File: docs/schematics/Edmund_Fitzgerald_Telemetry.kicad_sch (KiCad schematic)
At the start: 13 parts, among them Q1 MOSFET_N, Q2 MOSFET_N, U1 ESP32_Control, U2 MAX98357A, U3 DFPlayer_Pro

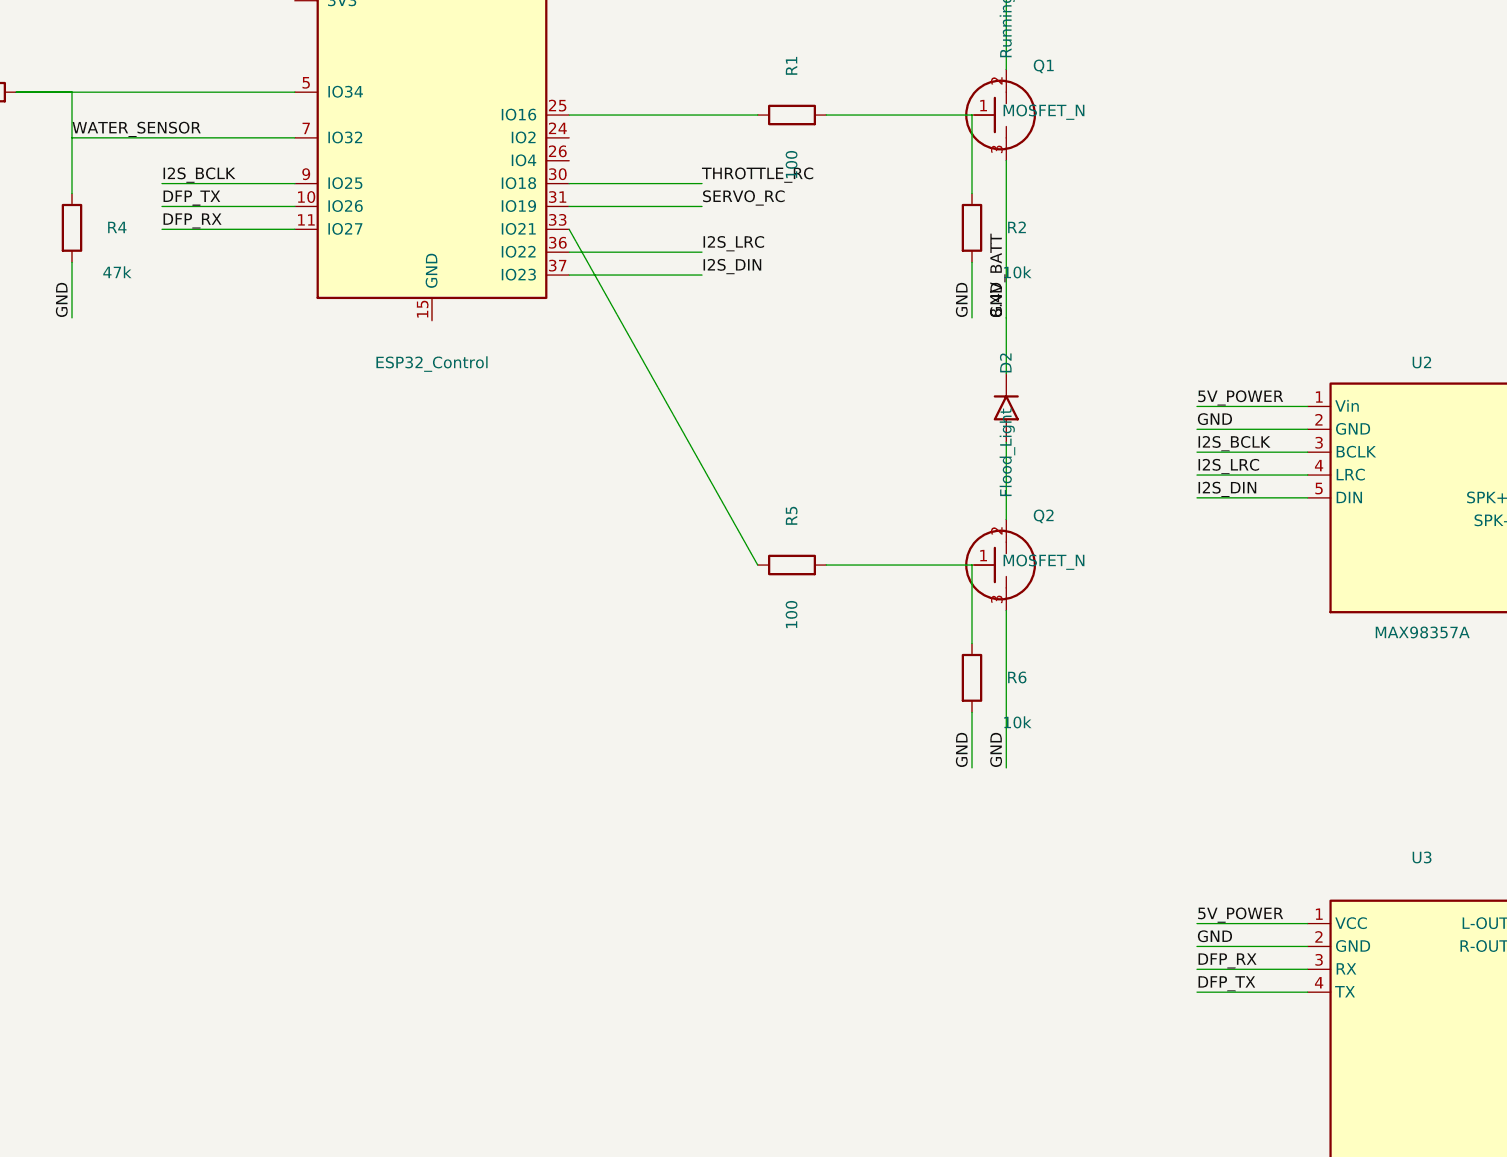
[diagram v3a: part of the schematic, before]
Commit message: Complete consolidated KiCAD schematic v3.0
- All components (ESP32, MOSFETs, Sensors, Audio) restored
- Physical orthogonal wiring between ESP32 and Audio modules
- Fixed all component labeling (no more ? symbols)
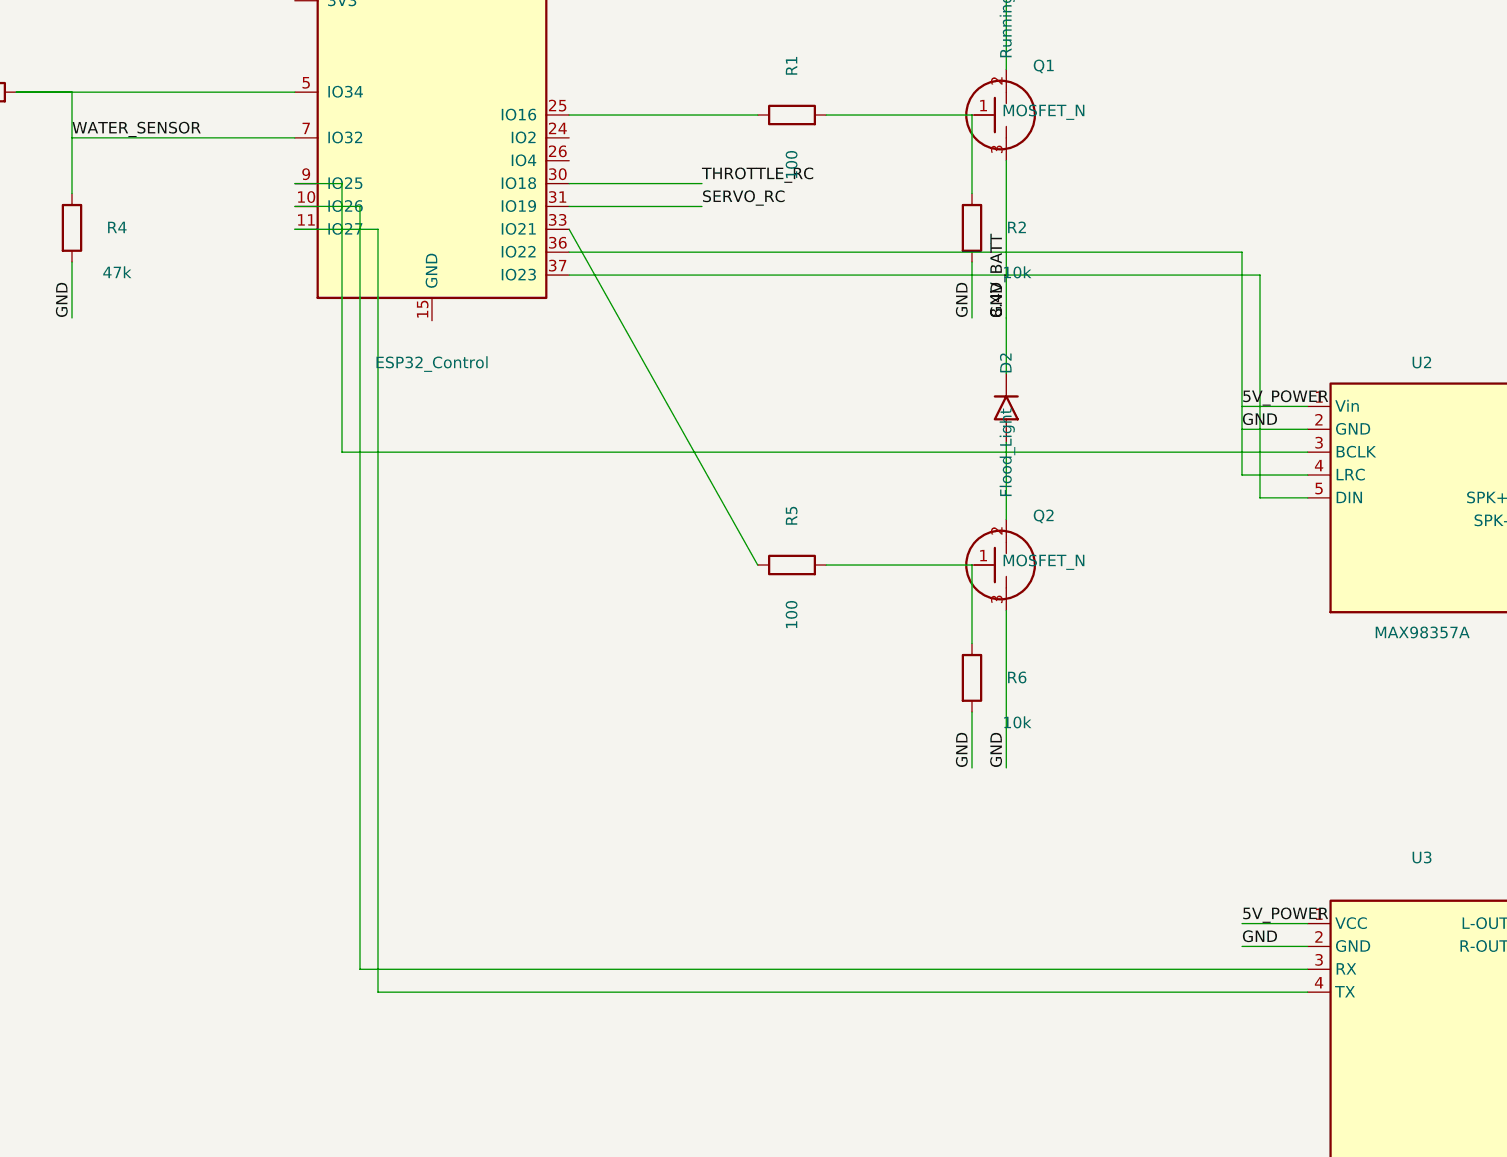
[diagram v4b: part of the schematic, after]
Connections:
- net 8.4V_BATT is gone; now on net 5V_POWER: D1.2 (A), D2.2 (A), Q1.3 (S), Q2.3 (S), R2.2, R3.1, R4.2, R6.2, U2.2 (GND), U3.2 (GND)
- net I2S_LRC is gone; now on net 5V_POWER: U1.36 (IO22), U2.4 (LRC)
- net DFP_RX: no longer names the net of U3.3 (RX)
- net DFP_RX: now also U1.10 (IO26); no longer U1.11 (IO27)
- net DFP_TX: no longer names the net of U3.4 (TX)
- net DFP_TX: now also U1.11 (IO27); no longer U1.10 (IO26)
- net I2S_BCLK: no longer names the net of U1.9 (IO25), U2.3 (BCLK)
- net I2S_DIN: no longer names the net of U1.37 (IO23), U2.5 (DIN)
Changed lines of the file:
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@@
 (kicad_sch (version 20230121) (generator eeschema)
  (paper "A3")
- (title_block (title "Edmund Fitzgerald - FULL SYSTEM") (company "Project Edmund Fitzgerald") (rev "2.0") (date "2026-01-31"))
+ (title_block (title "Edmund Fitzgerald - FULL SYSTEM") (company "Project Edmund Fitzgerald") (rev "2.3") (date "2026-01-31"))
  (symbol (lib_id "MCU_Espressif:ESP32-WROOM-32") (at 150 100 0) (unit 1) (in_bom yes) (on_board yes) (fields_autoplaced yes) (property "Reference" "U1" (at 150 75 0)) (property "Value" "ESP32_Control" (at 150 125 0)))
  (symbol (lib_id "Transistor_FET:Q_NMOS_GDS") (at 210 97.46 0) (unit 1) (in_bom yes) (on_board yes) (property "Reference" "Q1" (at 218 92 0)) (property "Value" "MOSFET_N" (at 218 97 0)))
@@
  (symbol (lib_id "Module:MAX98357A") (at 260 140 0) (unit 1) (in_bom yes) (on_board yes) (property "Reference" "U2" (at 260 125 0)) (property "Value" "MAX98357A" (at 260 155 0)))
  (symbol (lib_id "Module:DFPlayer_Pro") (at 260 200 0) (unit 1) (in_bom yes) (on_board yes) (property "Reference" "U3" (at 260 180 0)) (property "Value" "DFPlayer_Pro" (at 260 220 0)))
-  (wire (pts (xy 247.3 129.84) (xy 235 129.84)) (stroke (width 0) (type solid)))
-  (label "5V_POWER" (at 235 129.84 0) (effects (font (size 1.27 1.27)) (justify left bottom)))
-  (wire (pts (xy 247.3 132.38) (xy 235 132.38)) (stroke (width 0) (type solid)))
-  (label "GND" (at 235 132.38 0) (effects (font (size 1.27 1.27)) (justify left bottom)))
-  (wire (pts (xy 247.3 134.92) (xy 235 134.92)) (stroke (width 0) (type solid)))
-  (label "I2S_BCLK" (at 235 134.92 0) (effects (font (size 1.27 1.27)) (justify left bottom)))
-  (wire (pts (xy 247.3 137.46) (xy 235 137.46)) (stroke (width 0) (type solid)))
-  (label "I2S_LRC" (at 235 137.46 0) (effects (font (size 1.27 1.27)) (justify left bottom)))
-  (wire (pts (xy 247.3 140.0) (xy 235 140.0)) (stroke (width 0) (type solid)))
-  (label "I2S_DIN" (at 235 140.0 0) (effects (font (size 1.27 1.27)) (justify left bottom)))
-  (wire (pts (xy 247.3 187.3) (xy 235 187.3)) (stroke (width 0) (type solid)))
-  (label "5V_POWER" (at 235 187.3 0) (effects (font (size 1.27 1.27)) (justify left bottom)))
-  (wire (pts (xy 247.3 189.84) (xy 235 189.84)) (stroke (width 0) (type solid)))
-  (label "GND" (at 235 189.84 0) (effects (font (size 1.27 1.27)) (justify left bottom)))
-  (wire (pts (xy 247.3 192.38) (xy 235 192.38)) (stroke (width 0) (type solid)))
-  (label "DFP_RX" (at 235 192.38 0) (effects (font (size 1.27 1.27)) (justify left bottom)))
-  (wire (pts (xy 247.3 194.92) (xy 235 194.92)) (stroke (width 0) (type solid)))
-  (label "DFP_TX" (at 235 194.92 0) (effects (font (size 1.27 1.27)) (justify left bottom)))
-  (wire (pts (xy 134.76 105.08) (xy 120 105.08)) (stroke (width 0) (type solid)))
-  (label "I2S_BCLK" (at 120 105.08 0) (effects (font (size 1.27 1.27)) (justify left bottom)))
-  (wire (pts (xy 134.76 107.62) (xy 120 107.62)) (stroke (width 0) (type solid)))
-  (label "DFP_TX" (at 120 107.62 0) (effects (font (size 1.27 1.27)) (justify left bottom)))
-  (wire (pts (xy 134.76 110.16) (xy 120 110.16)) (stroke (width 0) (type solid)))
-  (label "DFP_RX" (at 120 110.16 0) (effects (font (size 1.27 1.27)) (justify left bottom)))
-  (wire (pts (xy 165.24 112.7) (xy 180 112.7)) (stroke (width 0) (type solid)))
-  (label "I2S_LRC" (at 180 112.7 0) (effects (font (size 1.27 1.27)) (justify left bottom)))
-  (wire (pts (xy 165.24 115.24) (xy 180 115.24)) (stroke (width 0) (type solid)))
-  (label "I2S_DIN" (at 180 115.24 0) (effects (font (size 1.27 1.27)) (justify left bottom)))
+  (wire (pts (xy 134.76 105.08) (xy 140 105.08)) (stroke (width 0) (type solid)))
+  (wire (pts (xy 140 105.08) (xy 140 134.92)) (stroke (width 0) (type solid)))
+  (wire (pts (xy 140 134.92) (xy 247.3 134.92)) (stroke (width 0) (type solid)))
+  (wire (pts (xy 165.24 112.7) (xy 240 112.7)) (stroke (width 0) (type solid)))
+  (wire (pts (xy 240 112.7) (xy 240 137.46)) (stroke (width 0) (type solid)))
+  (wire (pts (xy 240 137.46) (xy 247.3 137.46)) (stroke (width 0) (type solid)))
+  (wire (pts (xy 165.24 115.24) (xy 242 115.24)) (stroke (width 0) (type solid)))
+  (wire (pts (xy 242 115.24) (xy 242 140.0)) (stroke (width 0) (type solid)))
+  (wire (pts (xy 242 140.0) (xy 247.3 140.0)) (stroke (width 0) (type solid)))
+  (wire (pts (xy 134.76 107.62) (xy 142 107.62)) (stroke (width 0) (type solid)))
+  (wire (pts (xy 142 107.62) (xy 142 192.38)) (stroke (width 0) (type solid)))
+  (wire (pts (xy 142 192.38) (xy 247.3 192.38)) (stroke (width 0) (type solid)))
+  (wire (pts (xy 134.76 110.16) (xy 144 110.16)) (stroke (width 0) (type solid)))
+  (wire (pts (xy 144 110.16) (xy 144 194.92)) (stroke (width 0) (type solid)))
+  (wire (pts (xy 144 194.92) (xy 247.3 194.92)) (stroke (width 0) (type solid)))
+  (wire (pts (xy 247.3 129.84) (xy 240 129.84)) (stroke (width 0) (type solid)))
+  (label "5V_POWER" (at 240 129.84 0) (effects (font (size 1.27 1.27)) (justify left bottom)))
+  (wire (pts (xy 247.3 132.38) (xy 240 132.38)) (stroke (width 0) (type solid)))
+  (label "GND" (at 240 132.38 0) (effects (font (size 1.27 1.27)) (justify left bottom)))
+  (wire (pts (xy 247.3 187.3) (xy 240 187.3)) (stroke (width 0) (type solid)))
+  (label "5V_POWER" (at 240 187.3 0) (effects (font (size 1.27 1.27)) (justify left bottom)))
+  (wire (pts (xy 247.3 189.84) (xy 240 189.84)) (stroke (width 0) (type solid)))
+  (label "GND" (at 240 189.84 0) (effects (font (size 1.27 1.27)) (justify left bottom)))
   (wire (pts (xy 165.24 105.08) (xy 180 105.08)) (stroke (width 0) (type solid)))
   (label "THROTTLE_RC" (at 180 105.08 0) (effects (font (size 1.27 1.27)) (justify left bottom)))
@@
  (sheet_instances (path "/" (page "1")))
  (symbol_instances
-  (path "/7b7b4b12-bab1-4eb8-a1d9-e8ed2caabd69" (reference "U1") (unit 1) (value "ESP32_Control") (footprint ""))
-  (path "/252d442b-1aad-4156-9585-8b77ce3aff78" (reference "Q1") (unit 1) (value "MOSFET_N") (footprint ""))
-  (path "/b9955768-a1b3-4935-819a-0ea38235c3dc" (reference "R1") (unit 1) (value "100") (footprint ""))
-  (path "/947f2f4f-a5e5-475c-aca8-870b884c69b4" (reference "R2") (unit 1) (value "10k") (footprint ""))
-  (path "/e5060066-6f0d-44f5-aa65-96b8c167c61a" (reference "D1") (unit 1) (value "Running_Light") (footprint ""))
-  (path "/1539335d-5614-42ec-91c1-ec7cab45a6c0" (reference "Q2") (unit 1) (value "MOSFET_N") (footprint ""))
-  (path "/d822eb48-dbd7-47ed-9f6a-d0e75ebc0014" (reference "R5") (unit 1) (value "100") (footprint ""))
-  (path "/0c3a710e-1b05-4368-bc0d-6a548c5d18b4" (reference "R6") (unit 1) (value "10k") (footprint ""))
-  (path "/bf468513-f090-4156-9dce-d16bbbc43f35" (reference "D2") (unit 1) (value "Flood_Light") (footprint ""))
-  (path "/f2e21435-d765-4ddd-a21a-304409d59778" (reference "R3") (unit 1) (value "100k") (footprint ""))
-  (path "/7653210c-3678-4f00-89ea-94a9b4595bb1" (reference "R4") (unit 1) (value "47k") (footprint ""))
-  (path "/e63c4f07-211e-4934-a34b-ad3e5c7ada66" (reference "U2") (unit 1) (value "MAX98357A") (footprint ""))
-  (path "/2aa87f73-b4d4-4e42-a3ce-ffb6d8949e72" (reference "U3") (unit 1) (value "DFPlayer_Pro") (footprint ""))
+  (path "/9eaea18d-9522-43b2-81fe-d5eef67fb6b3" (reference "U1") (unit 1) (value "ESP32_Control") (footprint ""))
+  (path "/8cecb2ac-5490-4092-bcd3-be3b9cc41e31" (reference "Q1") (unit 1) (value "MOSFET_N") (footprint ""))
+  (path "/aca52501-c540-4fe5-9933-cb8ab05e2bf9" (reference "R1") (unit 1) (value "100") (footprint ""))
+  (path "/cd7e7c4d-5280-442e-ace4-f7e00b1d1cd3" (reference "R2") (unit 1) (value "10k") (footprint ""))
+  (path "/cdf19a2c-85c5-477e-8d29-e94ad4d8cdde" (reference "D1") (unit 1) (value "Running_Light") (footprint ""))
+  (path "/af116a73-7da3-4a81-aa4d-a6d183523ea6" (reference "Q2") (unit 1) (value "MOSFET_N") (footprint ""))
+  (path "/2a810406-33a5-48f1-8b9b-4e0ea532e60b" (reference "R5") (unit 1) (value "100") (footprint ""))
+  (path "/a4417c88-06ab-463e-bad3-de9ceef3a0ec" (reference "R6") (unit 1) (value "10k") (footprint ""))
+  (path "/eb3471c6-3048-4c1a-982f-aae1c3a2aa0a" (reference "D2") (unit 1) (value "Flood_Light") (footprint ""))
+  (path "/f80eeb1f-4947-4a81-8dba-3160fcefa8b7" (reference "R3") (unit 1) (value "100k") (footprint ""))
+  (path "/c14d0ece-557d-4618-847d-f14359060349" (reference "R4") (unit 1) (value "47k") (footprint ""))
+  (path "/36442b64-8740-42d5-ad09-1977904c5333" (reference "U2") (unit 1) (value "MAX98357A") (footprint ""))
+  (path "/ae061f74-8a18-40e4-84ad-10efb58106c8" (reference "U3") (unit 1) (value "DFPlayer_Pro") (footprint ""))
  )
 )

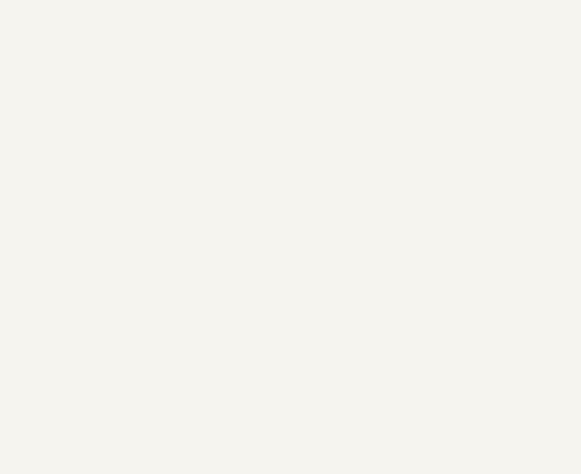
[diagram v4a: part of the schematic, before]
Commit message: Schematic update: Added ESP32-CAM module
- Added U4 ESP32-CAM module
- Added power connections for camera board
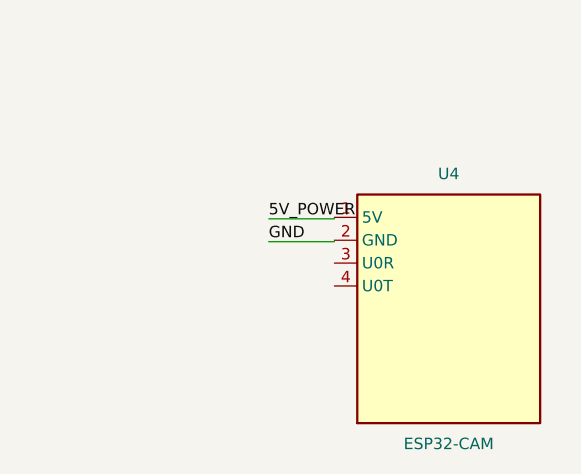
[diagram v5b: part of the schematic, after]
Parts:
- added U4: ESP32-CAM, symbol Module:ESP32-CAM
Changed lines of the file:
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@@
   (wire (pts (xy 165.24 107.62) (xy 180 107.62)) (stroke (width 0) (type solid)))
   (label "SERVO_RC" (at 180 107.62 0) (effects (font (size 1.27 1.27)) (justify left bottom)))
+ (symbol (lib_id "Module:ESP32-CAM") (at 260 260 0) (unit 1) (in_bom yes) (on_board yes) (property "Reference" "U4" (at 260 245 0)) (property "Value" "ESP32-CAM" (at 260 275 0)))
+  (wire (pts (xy 247.3 250) (xy 240 250)) (stroke (width 0) (type solid)))
+  (label "5V_POWER" (at 240 250 0) (effects (font (size 1.27 1.27)) (justify left bottom)))
+  (wire (pts (xy 247.3 252.54) (xy 240 252.54)) (stroke (width 0) (type solid)))
+  (label "GND" (at 240 252.54 0) (effects (font (size 1.27 1.27)) (justify left bottom)))
  (sheet_instances (path "/" (page "1")))
  (symbol_instances
-  (path "/9eaea18d-9522-43b2-81fe-d5eef67fb6b3" (reference "U1") (unit 1) (value "ESP32_Control") (footprint ""))
-  (path "/8cecb2ac-5490-4092-bcd3-be3b9cc41e31" (reference "Q1") (unit 1) (value "MOSFET_N") (footprint ""))
-  (path "/aca52501-c540-4fe5-9933-cb8ab05e2bf9" (reference "R1") (unit 1) (value "100") (footprint ""))
-  (path "/cd7e7c4d-5280-442e-ace4-f7e00b1d1cd3" (reference "R2") (unit 1) (value "10k") (footprint ""))
-  (path "/cdf19a2c-85c5-477e-8d29-e94ad4d8cdde" (reference "D1") (unit 1) (value "Running_Light") (footprint ""))
-  (path "/af116a73-7da3-4a81-aa4d-a6d183523ea6" (reference "Q2") (unit 1) (value "MOSFET_N") (footprint ""))
-  (path "/2a810406-33a5-48f1-8b9b-4e0ea532e60b" (reference "R5") (unit 1) (value "100") (footprint ""))
-  (path "/a4417c88-06ab-463e-bad3-de9ceef3a0ec" (reference "R6") (unit 1) (value "10k") (footprint ""))
-  (path "/eb3471c6-3048-4c1a-982f-aae1c3a2aa0a" (reference "D2") (unit 1) (value "Flood_Light") (footprint ""))
-  (path "/f80eeb1f-4947-4a81-8dba-3160fcefa8b7" (reference "R3") (unit 1) (value "100k") (footprint ""))
-  (path "/c14d0ece-557d-4618-847d-f14359060349" (reference "R4") (unit 1) (value "47k") (footprint ""))
-  (path "/36442b64-8740-42d5-ad09-1977904c5333" (reference "U2") (unit 1) (value "MAX98357A") (footprint ""))
-  (path "/ae061f74-8a18-40e4-84ad-10efb58106c8" (reference "U3") (unit 1) (value "DFPlayer_Pro") (footprint ""))
+  (path "/6a6324be-f0d9-4660-bc5d-eeee538c9470" (reference "U1") (unit 1) (value "ESP32_Control") (footprint ""))
+  (path "/e6c6d49d-ded3-45c0-8657-80a2199d261a" (reference "Q1") (unit 1) (value "MOSFET_N") (footprint ""))
+  (path "/9c377b0d-e973-464f-ba9b-c0d3ee695c13" (reference "R1") (unit 1) (value "100") (footprint ""))
+  (path "/7128e088-a8e0-42b0-9125-83b782143666" (reference "R2") (unit 1) (value "10k") (footprint ""))
+  (path "/d0d04165-f706-4efb-a5ed-0caab7ad5f03" (reference "D1") (unit 1) (value "Running_Light") (footprint ""))
+  (path "/92d89f8a-660c-417e-aec4-9fac9af41bea" (reference "Q2") (unit 1) (value "MOSFET_N") (footprint ""))
+  (path "/e6ae053f-17f8-4cfd-a3d7-8c2b0e82cf8d" (reference "R5") (unit 1) (value "100") (footprint ""))
+  (path "/eb2263f6-fe29-44c1-9933-d479aa6b8725" (reference "R6") (unit 1) (value "10k") (footprint ""))
+  (path "/6b753ff5-9ad9-4527-975b-9cd45fada08d" (reference "D2") (unit 1) (value "Flood_Light") (footprint ""))
+  (path "/ee19817b-94e3-4076-bef5-0ab82a0e50dd" (reference "R3") (unit 1) (value "100k") (footprint ""))
+  (path "/9b2eb7d3-e64b-4f15-a07f-808149288232" (reference "R4") (unit 1) (value "47k") (footprint ""))
+  (path "/c80a82f1-7912-4ad3-b0df-f396f591f5cb" (reference "U2") (unit 1) (value "MAX98357A") (footprint ""))
+  (path "/81f42d43-b268-4c93-8496-6c3cabc9e4f4" (reference "U3") (unit 1) (value "DFPlayer_Pro") (footprint ""))
+  (path "/73432528-8c83-4b83-9f07-bf1c70c183ea" (reference "U4") (unit 1) (value "ESP32-CAM") (footprint ""))
  )
 )
